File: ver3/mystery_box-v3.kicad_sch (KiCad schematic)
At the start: 56 parts, among them J1 Screw_Terminal_01x02, J10 Screw_Terminal_01x02, J11 Screw_Terminal_01x02, J12 Screw_Terminal_01x02, J13 Screw_Terminal_01x02, J14 Screw_Terminal_01x02, J15 Screw_Terminal_01x02, J16 Screw_Terminal_01x02, J17 Screw_Terminal_01x02, J18 Barrel_Jack_MountingPin, J20 rj45-CC-X2-Aliexpress, J8 Screw_Terminal_01x02, J9 Screw_Terminal_01x02, Q1 IRLZ44N, Q2 IRLZ44N, Q3 IRLZ44N

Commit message: beginning ver3 PCB
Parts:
- GPIO13_SERIAL1: renamed from GPIO13_SERIAL2; footprint (none) -> Connector_PinHeader_2.54mm:PinHeader_1x03_P2.54mm_Vertical
- GPIO_CONN1: footprint (none) -> Connector_PinHeader_2.54mm:PinHeader_1x04_P2.54mm_Vertical
- JMP_24V_12V_POE1: renamed from GPIO13_SERIAL1; footprint (none) -> Connector_PinHeader_2.54mm:PinHeader_1x03_P2.54mm_Vertical
- JMP_5V_USB-BUCK1: footprint (none) -> Connector_PinHeader_2.54mm:PinHeader_1x02_P2.54mm_Vertical
- JMP_BUCK_PWR1, JMP_NEO1_PWR1, JMP_NEO2_PWR1, JMP_NEO3_PWR1: footprint (none) -> Connector_PinHeader_2.54mm:PinHeader_1x03_P2.54mm_Vertical
- M1: value ~ -> 24V-Boost-Converter; footprint (none) -> eigene_footprints:24V Boost Converter
- M2: footprint (none) -> eigene_footprints:5V Buck Converter
- NEO_T1, NEO_T2, NEO_T3: footprint (none) -> TerminalBlock:TerminalBlock_MaiXu_MX126-5.0-03P_1x03_P5.00mm
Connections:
- net GND: now also M1.3 (IN-), M1.5 (OUT-), M1.6 (OUT-), M2.3 (IN-), M2.5 (OUT-), M2.6 (OUT-); no longer M1.2 (IN-), M2.2 (IN-)
- net VCC 12V: now also M1.2 (IN+)
- net VCC 5V BUCK: now also M2.7 (OUT+), M2.8 (OUT+); no longer M2.3 (OUT+)
- net VCC 24V: now reaches JMP_24V_12V_POE1.3 (Pin_3)
- net VCC 24V: now also M1.7 (OUT+), M1.8 (OUT+); no longer M1.3 (OUT+)
- net at JMP_BUCK_PWR1.2 (Pin_2), M2.1 (IN+): now also M2.2 (IN+)
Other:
- moved on the sheet: GPIO13_SERIAL1

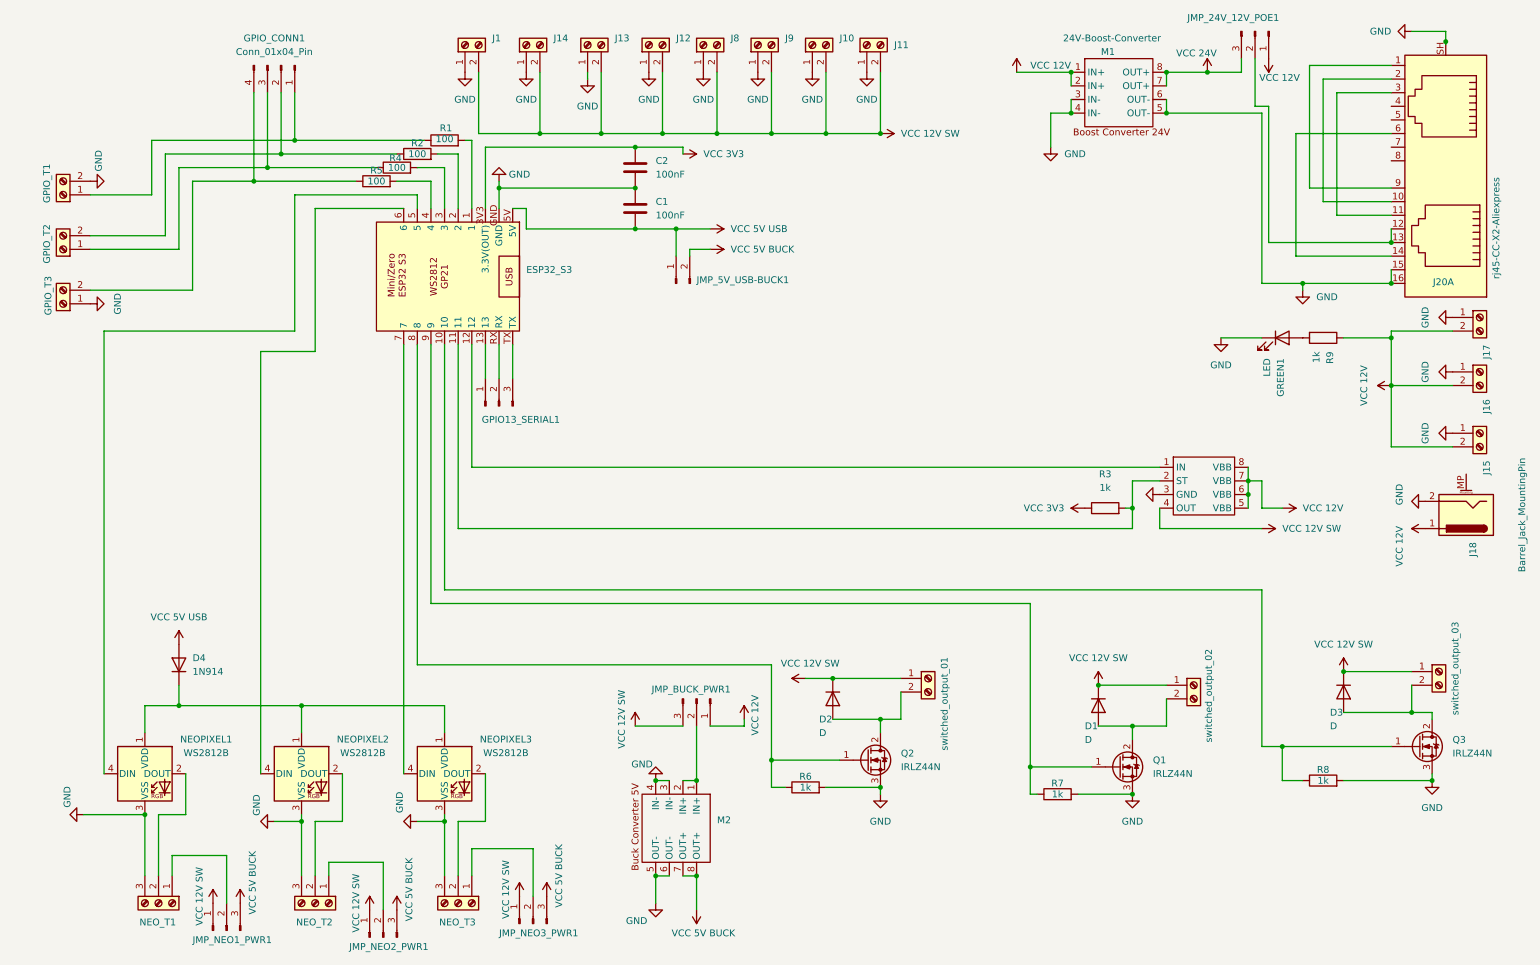
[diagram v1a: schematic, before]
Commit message: readded DMX
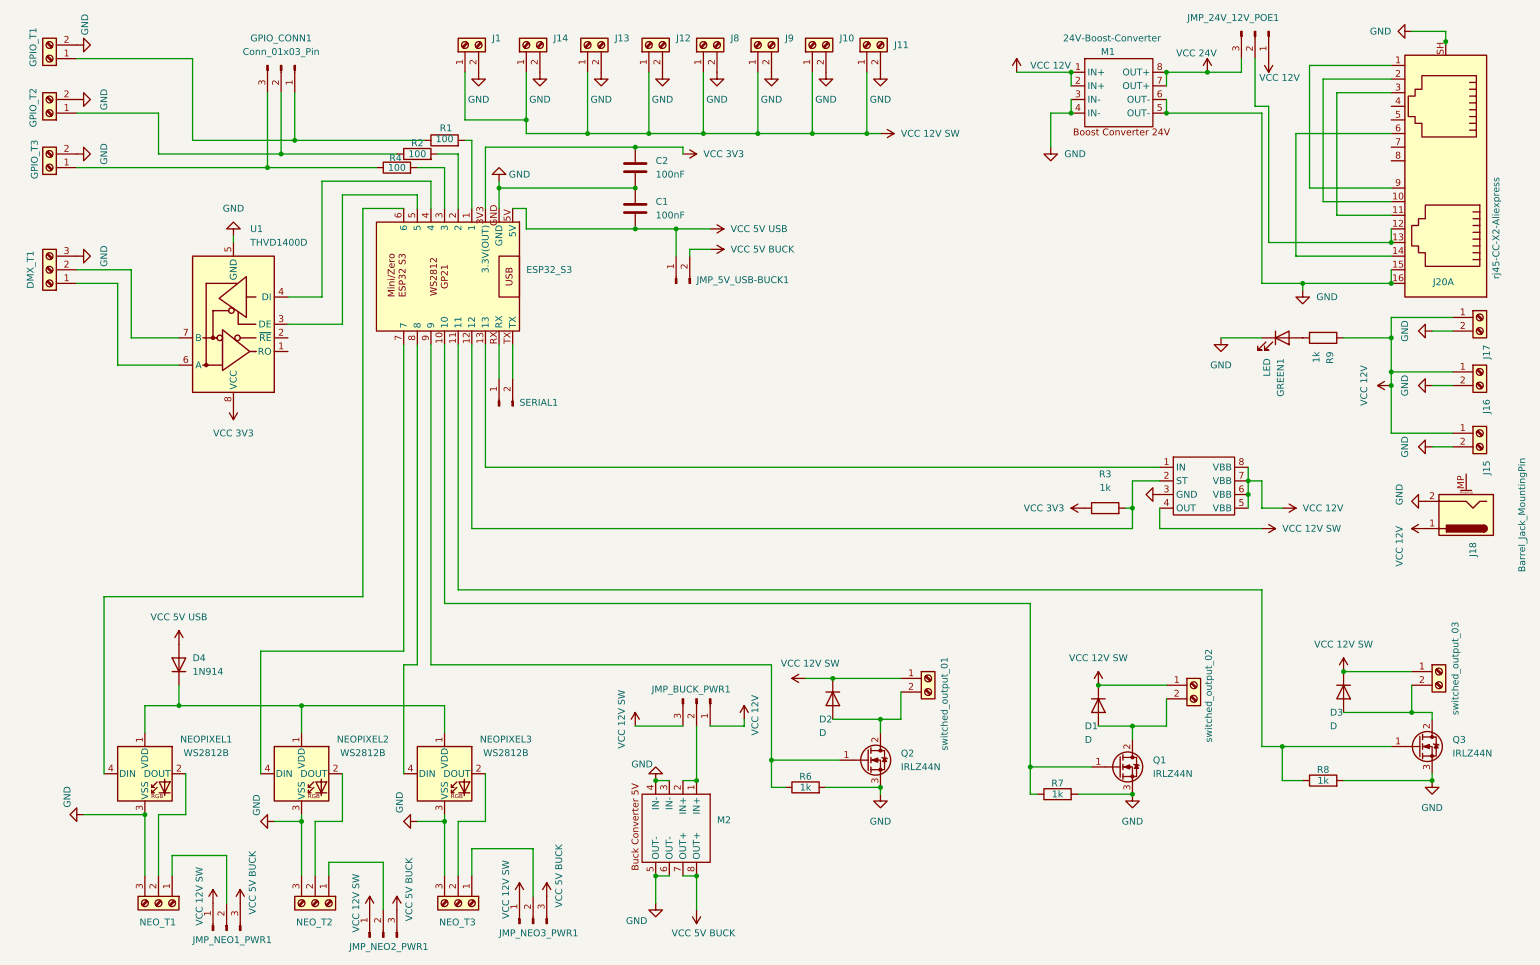
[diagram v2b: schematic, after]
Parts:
- removed GPIO13_SERIAL1: Conn_01x03_Pin, Connector_PinHeader_2.54mm:PinHeader_1x03_P2.54mm_Vertical, symbol Connector:Conn_01x03_Pin
- removed GPIO_CONN1: Conn_01x04_Pin, Connector_PinHeader_2.54mm:PinHeader_1x04_P2.54mm_Vertical, symbol Connector:Conn_01x04_Pin
- removed R5: 100, Resistor_THT:R_Axial_DIN0207_L6.3mm_D2.5mm_P10.16mm_Horizontal, symbol Device:R
- added DMX_T1: Screw_Terminal_01x03, TerminalBlock:TerminalBlock_MaiXu_MX126-5.0-03P_1x03_P5.00mm, symbol Connector:Screw_Terminal_01x03
- added GPIO_CONN1: Conn_01x03_Pin, Connector_PinHeader_2.54mm:PinHeader_1x03_P2.54mm_Vertical, symbol Connector:Conn_01x03_Pin
- added SERIAL1: Conn_01x02_Pin, Connector_PinHeader_2.54mm:PinHeader_1x02_P2.54mm_Vertical, symbol Connector:Conn_01x02_Pin
- added U1: THVD1400D, Package_SO:SOIC-8_3.9x4.9mm_P1.27mm, symbol Interface_UART:THVD1400D
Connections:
- net GND: now also GPIO_T2.2 (Pin_2), GPIO_T3.2 (Pin_2), J1.2 (Pin_2), J10.2 (Pin_2), J11.2 (Pin_2), J12.2 (Pin_2), J13.2 (Pin_2), J14.2 (Pin_2), J15.2 (Pin_2), J16.2 (Pin_2), J17.2 (Pin_2), J8.2 (Pin_2), J9.2 (Pin_2), DMX_T1.3 (Pin_3), U1.5 (GND); no longer GPIO_T3.1 (Pin_1), J1.1 (Pin_1), J10.1 (Pin_1), J11.1 (Pin_1), J12.1 (Pin_1), J13.1 (Pin_1), J14.1 (Pin_1), J15.1 (Pin_1), J16.1 (Pin_1), J17.1 (Pin_1), J8.1 (Pin_1), J9.1 (Pin_1)
- net VCC 12V: now also J15.1 (Pin_1), J16.1 (Pin_1), J17.1 (Pin_1); no longer J15.2 (Pin_2), J16.2 (Pin_2), J17.2 (Pin_2)
- net VCC 12V SW: now also J1.1 (Pin_1), J10.1 (Pin_1), J11.1 (Pin_1), J12.1 (Pin_1), J13.1 (Pin_1), J14.1 (Pin_1), J8.1 (Pin_1), J9.1 (Pin_1); no longer J1.2 (Pin_2), J10.2 (Pin_2), J11.2 (Pin_2), J12.2 (Pin_2), J13.2 (Pin_2), J14.2 (Pin_2), J8.2 (Pin_2), J9.2 (Pin_2)
- net VCC 3V3: now also U1.8 (VCC)
- net at Q3.1 (G), R8.1: now also ESP32_S3.11; no longer ESP32_S3.10
- net at R3.2, U3.2 (ST): now also ESP32_S3.12; no longer ESP32_S3.11
- net at U3.1 (IN): now also ESP32_S3.13; no longer ESP32_S3.12
- net at ESP32_S3.4: now also U1.4 (DI)
- net at ESP32_S3.5: now also U1.3 (DE); no longer NEOPIXEL1.4 (DIN)
- net at ESP32_S3.6: now also NEOPIXEL1.4 (DIN); no longer NEOPIXEL2.4 (DIN)
- net at ESP32_S3.7: now also NEOPIXEL2.4 (DIN); no longer NEOPIXEL3.4 (DIN)
- net at Q2.1 (G), R6.1: now also ESP32_S3.9; no longer ESP32_S3.8
- net at Q1.1 (G), R7.1: now also ESP32_S3.10; no longer ESP32_S3.9
- net at ESP32_S3.RX: now also SERIAL1.1 (Pin_1)
- net at ESP32_S3.TX: now also SERIAL1.2 (Pin_2)
- net at R4.1: now also GPIO_T3.1 (Pin_1), GPIO_CONN1.3 (Pin_3); no longer GPIO_T2.1 (Pin_1)
- net at GPIO_T1.1 (Pin_1), R1.1: now also GPIO_CONN1.1 (Pin_1)
- net at R2.1: now also GPIO_T2.1 (Pin_1), GPIO_CONN1.2 (Pin_2); no longer GPIO_T2.2 (Pin_2)
- new net: ESP32_S3.8, NEOPIXEL3.4 (DIN)
- new net: DMX_T1.1 (Pin_1), U1.6 (A)
- new net: DMX_T1.2 (Pin_2), U1.7 (B)
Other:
- moved on the sheet: GPIO_T1, GPIO_T2, GPIO_T3

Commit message: ver3: first PCB layout
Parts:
- DMX_T1, NEO_T1, NEO_T2, NEO_T3: symbol Connector:Screw_Terminal_01x03 -> eigene:Screw_Terminal_01x03
- GPIO_T1, GPIO_T2, GPIO_T3, J1, J10, J11, J12, J13, J14, J15, J16, J17, J8, J9, switched_output_01, switched_output_02, switched_output_03: symbol Connector:Screw_Terminal_01x02 -> eigene:Screw_Terminal_01x02
- R6, R7, R8: value 1k -> 10k
- renumbered D2 to D1, D1 to D2, Q2 to Q1, Q1 to Q2
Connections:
- net GND: now also DMX_T1.1 (Pin_3), GPIO_T1.1 (Pin_2), GPIO_T2.1 (Pin_2), GPIO_T3.1 (Pin_2), J1.1 (Pin_2), J10.1 (Pin_2), J11.1 (Pin_2), J12.1 (Pin_2), J13.1 (Pin_2), J14.1 (Pin_2), J15.1 (Pin_2), J16.1 (Pin_2), J17.1 (Pin_2), J8.1 (Pin_2), J9.1 (Pin_2), NEO_T1.1 (Pin_3), NEO_T2.1 (Pin_3), NEO_T3.1 (Pin_3); no longer DMX_T1.3 (Pin_3), GPIO_T1.2 (Pin_2), GPIO_T2.2 (Pin_2), GPIO_T3.2 (Pin_2), J1.2 (Pin_2), J10.2 (Pin_2), J11.2 (Pin_2), J12.2 (Pin_2), J13.2 (Pin_2), J14.2 (Pin_2), J15.2 (Pin_2), J16.2 (Pin_2), J17.2 (Pin_2), J8.2 (Pin_2), J9.2 (Pin_2), NEO_T1.3 (Pin_3), NEO_T2.3 (Pin_3), NEO_T3.3 (Pin_3)
- net VCC 12V: now also J15.2 (Pin_1), J16.2 (Pin_1), J17.2 (Pin_1); no longer J15.1 (Pin_1), J16.1 (Pin_1), J17.1 (Pin_1)
- net VCC 12V SW: now also J1.2 (Pin_1), J10.2 (Pin_1), J11.2 (Pin_1), J12.2 (Pin_1), J13.2 (Pin_1), J14.2 (Pin_1), J8.2 (Pin_1), J9.2 (Pin_1), switched_output_01.2 (Pin_1), switched_output_02.2 (Pin_1), switched_output_03.2 (Pin_1); no longer J1.1 (Pin_1), J10.1 (Pin_1), J11.1 (Pin_1), J12.1 (Pin_1), J13.1 (Pin_1), J14.1 (Pin_1), J8.1 (Pin_1), J9.1 (Pin_1), switched_output_01.1 (Pin_1), switched_output_02.1 (Pin_1), switched_output_03.1 (Pin_1)
- net at JMP_NEO3_PWR1.2 (Pin_2): now also NEO_T3.3 (Pin_1); no longer NEO_T3.1 (Pin_1)
- net at JMP_NEO1_PWR1.2 (Pin_2): now also NEO_T1.3 (Pin_1); no longer NEO_T1.1 (Pin_1)
- net at U1.6 (A): now also DMX_T1.3 (Pin_1); no longer DMX_T1.1 (Pin_1)
- net at GPIO_CONN1.3 (Pin_3), R4.1: now also GPIO_T3.2 (Pin_1); no longer GPIO_T3.1 (Pin_1)
- net at JMP_NEO2_PWR1.2 (Pin_2): now also NEO_T2.3 (Pin_1); no longer NEO_T2.1 (Pin_1)
- net at D2.2 (A), Q2.2 (D): now also switched_output_02.1 (Pin_2); no longer switched_output_02.2 (Pin_2)
- net at D1.2 (A), Q1.2 (D): now also switched_output_01.1 (Pin_2); no longer switched_output_01.2 (Pin_2)
- net at D3.2 (A), Q3.2 (D): now also switched_output_03.1 (Pin_2); no longer switched_output_03.2 (Pin_2)
- net at GPIO_CONN1.1 (Pin_1), R1.1: now also GPIO_T1.2 (Pin_1); no longer GPIO_T1.1 (Pin_1)
- net at GPIO_CONN1.2 (Pin_2), R2.1: now also GPIO_T2.2 (Pin_1); no longer GPIO_T2.1 (Pin_1)
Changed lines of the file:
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@@
 	)
 	(symbol
-		(lib_id "Connector:Screw_Terminal_01x02")
+		(lib_id "eigene:Screw_Terminal_01x02")
 		(at 156.21 19.05 90)
 		(unit 1)
@@
 		(fields_autoplaced yes)
 		(property "Reference" "J10"
-			(at 161.29 17.7799 90)
+			(at 161.29 19.0499 90)
 			(effects
 				(font
@@
 	)
 	(symbol
-		(lib_id "Connector:Screw_Terminal_01x02")
+		(lib_id "eigene:Screw_Terminal_01x02")
 		(at 280.67 69.85 0)
 		(unit 1)
@@
 		(fields_autoplaced yes)
 		(property "Reference" "J17"
-			(at 281.9401 74.93 90)
+			(at 283.21 71.1199 0)
 			(effects
 				(font
 					(size 1.27 1.27)
 				)
-				(justify right)
+				(justify left)
 			)
 		)
@@
 	)
 	(symbol
-		(lib_id "Connector:Screw_Terminal_01x02")
+		(lib_id "eigene:Screw_Terminal_01x02")
 		(at 125.73 19.05 90)
 		(unit 1)
@@
 		(fields_autoplaced yes)
 		(property "Reference" "J12"
-			(at 130.81 17.7799 90)
+			(at 130.81 19.0499 90)
 			(effects
 				(font
@@
 	)
 	(symbol
-		(lib_id "Connector:Screw_Terminal_01x02")
+		(lib_id "eigene:Screw_Terminal_01x02")
 		(at 102.87 19.05 90)
 		(unit 1)
@@
 		(fields_autoplaced yes)
 		(property "Reference" "J14"
-			(at 107.95 17.7799 90)
+			(at 107.95 19.0499 90)
 			(effects
 				(font
@@
 	)
 	(symbol
-		(lib_id "Connector:Screw_Terminal_01x03")
+		(lib_id "eigene:Screw_Terminal_01x03")
 		(at 63.5 179.07 270)
 		(unit 1)
@@
 	)
 	(symbol
-		(lib_id "Connector:Screw_Terminal_01x02")
+		(lib_id "eigene:Screw_Terminal_01x02")
 		(at 135.89 19.05 90)
 		(unit 1)
@@
 		(fields_autoplaced yes)
 		(property "Reference" "J8"
-			(at 140.97 17.7799 90)
+			(at 140.97 19.0499 90)
 			(effects
 				(font
@@
 	)
 	(symbol
-		(lib_id "Connector:Screw_Terminal_01x02")
+		(lib_id "eigene:Screw_Terminal_01x02")
 		(at 13.97 41.91 180)
 		(unit 1)
@@
 	)
 	(symbol
-		(lib_id "Connector:Screw_Terminal_01x02")
+		(lib_id "eigene:Screw_Terminal_01x02")
 		(at 227.33 138.43 0)
 		(unit 1)
@@
 		(dnp no)
 		(fields_autoplaced yes)
-		(property "Reference" "Q1"
+		(property "Reference" "Q2"
 			(at 219.71 152.3999 0)
 			(effects
@@
 			(project ""
 				(path "/cbbaaa27-ed93-4129-abc1-94959947e6fe"
-					(reference "Q1")
+					(reference "Q2")
 					(unit 1)
 				)
@@
 		(dnp no)
 		(fields_autoplaced yes)
-		(property "Reference" "Q2"
+		(property "Reference" "Q1"
 			(at 172.72 151.1299 0)
 			(effects
@@
 			(project "mystery_box-v3"
 				(path "/cbbaaa27-ed93-4129-abc1-94959947e6fe"
-					(reference "Q2")
+					(reference "Q1")
 					(unit 1)
 				)
@@
 	)
 	(symbol
-		(lib_id "Connector:Screw_Terminal_01x02")
+		(lib_id "eigene:Screw_Terminal_01x02")
 		(at 273.05 135.89 0)
 		(unit 1)
@@
 			)
 		)
-		(property "Value" "1k"
+		(property "Value" "10k"
 			(at 154.94 157.48 90)
 			(effects
@@
 		(on_board yes)
 		(dnp no)
-		(property "Reference" "D1"
+		(property "Reference" "D2"
 			(at 207.01 146.0499 90)
 			(effects
@@
 			(project ""
 				(path "/cbbaaa27-ed93-4129-abc1-94959947e6fe"
-					(reference "D1")
+					(reference "D2")
 					(unit 1)
 				)
@@
 	)
 	(symbol
-		(lib_id "Connector:Screw_Terminal_01x02")
+		(lib_id "eigene:Screw_Terminal_01x02")
 		(at 280.67 91.44 0)
 		(unit 1)
@@
 		(fields_autoplaced yes)
 		(property "Reference" "J15"
-			(at 281.9401 96.52 90)
+			(at 283.21 92.7099 0)
 			(effects
 				(font
 					(size 1.27 1.27)
 				)
-				(justify right)
+				(justify left)
 			)
 		)
@@
 	)
 	(symbol
-		(lib_id "Connector:Screw_Terminal_01x03")
+		(lib_id "eigene:Screw_Terminal_01x03")
 		(at 90.17 179.07 270)
 		(unit 1)
@@
 	)
 	(symbol
-		(lib_id "Connector:Screw_Terminal_01x02")
+		(lib_id "eigene:Screw_Terminal_01x02")
 		(at 166.37 19.05 90)
 		(unit 1)
@@
 	)
 	(symbol
-		(lib_id "Connector:Screw_Terminal_01x02")
+		(lib_id "eigene:Screw_Terminal_01x02")
 		(at 146.05 19.05 90)
 		(unit 1)
@@
 		(fields_autoplaced yes)
 		(property "Reference" "J9"
-			(at 151.13 17.7799 90)
+			(at 151.13 19.0499 90)
 			(effects
 				(font
@@
 	)
 	(symbol
-		(lib_id "Connector:Screw_Terminal_01x02")
+		(lib_id "eigene:Screw_Terminal_01x02")
 		(at 13.97 21.59 180)
 		(unit 1)
@@
 			)
 		)
-		(property "Value" "1k"
+		(property "Value" "10k"
 			(at 201.93 158.75 90)
 			(effects
@@
 	)
 	(symbol
-		(lib_id "Connector:Screw_Terminal_01x02")
+		(lib_id "eigene:Screw_Terminal_01x02")
 		(at 114.3 19.05 90)
 		(unit 1)
@@
 		(fields_autoplaced yes)
 		(property "Reference" "J13"
-			(at 119.38 17.7799 90)
+			(at 119.38 19.0499 90)
 			(effects
 				(font
@@
 	)
 	(symbol
-		(lib_id "Connector:Screw_Terminal_01x02")
+		(lib_id "eigene:Screw_Terminal_01x02")
 		(at 177.8 137.16 0)
 		(unit 1)
@@
 	)
 	(symbol
-		(lib_id "Connector:Screw_Terminal_01x02")
+		(lib_id "eigene:Screw_Terminal_01x02")
 		(at 13.97 31.75 180)
 		(unit 1)
@@
 	)
 	(symbol
-		(lib_id "Connector:Screw_Terminal_01x02")
+		(lib_id "eigene:Screw_Terminal_01x02")
 		(at 280.67 80.01 0)
 		(unit 1)
@@
 		(fields_autoplaced yes)
 		(property "Reference" "J16"
-			(at 281.9401 85.09 90)
+			(at 283.21 81.2799 0)
 			(effects
 				(font
 					(size 1.27 1.27)
 				)
-				(justify right)
+				(justify left)
 			)
 		)
@@
 		(on_board yes)
 		(dnp no)
-		(property "Reference" "D2"
+		(property "Reference" "D1"
 			(at 157.48 144.7799 90)
 			(effects
@@
 			(project "mystery_box-v3"
 				(path "/cbbaaa27-ed93-4129-abc1-94959947e6fe"
-					(reference "D2")
+					(reference "D1")
 					(unit 1)
 				)
@@
 	)
 	(symbol
-		(lib_id "Connector:Screw_Terminal_01x03")
+		(lib_id "eigene:Screw_Terminal_01x03")
 		(at 34.29 179.07 270)
 		(unit 1)
@@
 			)
 		)
-		(property "Value" "1k"
+		(property "Value" "10k"
 			(at 251.46 156.21 90)
 			(effects
@@
 	)
 	(symbol
-		(lib_id "Connector:Screw_Terminal_01x03")
+		(lib_id "eigene:Screw_Terminal_01x03")
 		(at 13.97 60.96 180)
 		(unit 1)
@@
 	)
 	(symbol
-		(lib_id "Connector:Screw_Terminal_01x02")
+		(lib_id "eigene:Screw_Terminal_01x02")
 		(at 91.44 19.05 90)
 		(unit 1)
@@
 		(fields_autoplaced yes)
 		(property "Reference" "J1"
-			(at 96.52 17.7799 90)
+			(at 96.52 19.0499 90)
 			(effects
 				(font

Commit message: beginning ver3 PCB routing
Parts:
- added J2: XLR3, Connector_Audio:Jack_XLR_Neutrik_NC3FAAH-0_Horizontal, symbol Connector_Audio:XLR3
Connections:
- net GND: now also J2.1
- net VCC 3V3: now also U1.2 (~{RE}), U1.3 (DE)
- net at ESP32_S3.5: no longer U1.3 (DE)
- net at DMX_T1.3 (Pin_1), U1.6 (A): now also J2.3
- net at DMX_T1.2 (Pin_2), U1.7 (B): now also J2.2

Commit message: logo + silk stuff
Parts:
- added PWR_12V_FAN: Conn_01x02_Pin, Connector_PinHeader_2.54mm:PinHeader_1x02_P2.54mm_Vertical, symbol Connector:Conn_01x02_Pin
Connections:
- net GND: now also PWR_12V_FAN.2 (Pin_2)
- net VCC 12V: now also PWR_12V_FAN.1 (Pin_1)
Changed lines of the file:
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@@
 	)
 	(junction
+		(at 264.16 87.63)
+		(diameter 0)
+		(color 0 0 0 0)
+	)
+	(junction
 		(at 264.16 82.55)
 		(diameter 0)
@@
 	(wire
 		(pts
+			(xy 254 90.17) (xy 254 92.71)
+		)
+		(stroke
+			(width 0)
+			(type default)
+		)
+	)
+	(wire
+		(pts
 			(xy 251.46 25.4) (xy 251.46 48.26)
 		)
@@
 	(wire
 		(pts
-			(xy 264.16 82.55) (xy 264.16 91.44)
+			(xy 264.16 82.55) (xy 264.16 87.63)
 		)
 		(stroke
@@
 	(wire
 		(pts
+			(xy 251.46 90.17) (xy 254 90.17)
+		)
+		(stroke
+			(width 0)
+			(type default)
+		)
+	)
+	(wire
+		(pts
 			(xy 161.29 152.4) (xy 148.59 152.4)
 		)
@@
 	(wire
 		(pts
+			(xy 264.16 87.63) (xy 264.16 91.44)
+		)
+		(stroke
+			(width 0)
+			(type default)
+		)
+	)
+	(wire
+		(pts
 			(xy 95.25 38.1) (xy 95.25 49.53)
 		)
@@
 	(wire
 		(pts
+			(xy 251.46 87.63) (xy 264.16 87.63)
+		)
+		(stroke
+			(width 0)
+			(type default)
+		)
+	)
+	(wire
+		(pts
 			(xy 92.71 74.93) (xy 92.71 109.22)
 		)
@@
 	)
 	(symbol
+		(lib_id "Connector:Conn_01x02_Pin")
+		(at 246.38 87.63 0)
+		(unit 1)
+		(exclude_from_sim no)
+		(in_bom yes)
+		(on_board yes)
+		(dnp no)
+		(property "Reference" "PWR_12V_FAN"
+			(at 247.0151 91.44 0)
+			(effects
+				(font
+					(size 1.27 1.27)
+				)
+				(justify right)
+			)
+		)
+		(property "Value" "Conn_01x02_Pin"
+			(at 245.7451 91.44 90)
+			(effects
+				(font
+					(size 1.27 1.27)
+				)
+				(justify right)
+				(hide yes)
+			)
+		)
+		(property "Footprint" "Connector_PinHeader_2.54mm:PinHeader_1x02_P2.54mm_Vertical"
+			(at 246.38 87.63 0)
+			(effects
+				(font
+					(size 1.27 1.27)
+				)
+				(hide yes)
+			)
+		)
+		(property "Datasheet" "~"
+			(at 246.38 87.63 0)
+			(effects
+				(font
+					(size 1.27 1.27)
+				)
+				(hide yes)
+			)
+		)
+		(property "Description" "Generic connector, single row, 01x02, script generated"
+			(at 246.38 87.63 0)
+			(effects
+				(font
+					(size 1.27 1.27)
+				)
+				(hide yes)
+			)
+		)
+		(pin "2"
+		)
+		(pin "1"
+		)
+		(instances
+			(project "mystery_box-v3"
+				(path "/cbbaaa27-ed93-4129-abc1-94959947e6fe"
+					(reference "PWR_12V_FAN")
+					(unit 1)
+				)
+			)
+		)
+	)
+	(symbol
 		(lib_id "eigene:Screw_Terminal_01x02")
 		(at 227.33 138.43 0)
@@
 	)
 	(symbol
+		(lib_id "power:GND")
+		(at 254 92.71 0)
+		(unit 1)
+		(exclude_from_sim no)
+		(in_bom yes)
+		(on_board yes)
+		(dnp no)
+		(fields_autoplaced yes)
+		(property "Reference" "#PWR060"
+			(at 254 99.06 0)
+			(effects
+				(font
+					(size 1.27 1.27)
+				)
+				(hide yes)
+			)
+		)
+		(property "Value" "GND"
+			(at 254 97.79 0)
+			(effects
+				(font
+					(size 1.27 1.27)
+				)
+			)
+		)
+		(property "Footprint" ""
+			(at 254 92.71 0)
+			(effects
+				(font
+					(size 1.27 1.27)
+				)
+				(hide yes)
+			)
+		)
+		(property "Datasheet" ""
+			(at 254 92.71 0)
+			(effects
+				(font
+					(size 1.27 1.27)
+				)
+				(hide yes)
+			)
+		)
+		(property "Description" "Power symbol creates a global label with name \"GND\" , ground"
+			(at 254 92.71 0)
+			(effects
+				(font
+					(size 1.27 1.27)
+				)
+				(hide yes)
+			)
+		)
+		(pin "1"
+		)
+		(instances
+			(project "mystery_box-v3"
+				(path "/cbbaaa27-ed93-4129-abc1-94959947e6fe"
+					(reference "#PWR060")
+					(unit 1)
+				)
+			)
+		)
+	)
+	(symbol
 		(lib_id "power:VCC")
 		(at 106.68 177.8 0)
@@
 		(on_board yes)
 		(dnp no)
-		(fields_autoplaced yes)
 		(property "Reference" "GREEN1"
 			(at 243.5226 77.47 90)
